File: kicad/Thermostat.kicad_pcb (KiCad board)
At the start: 4 copper layers, 82 x 46 mm, 5 parts, among them J1 Conn_02x20_Odd_Even, U3 XIAO-ESP32-C6-SMD

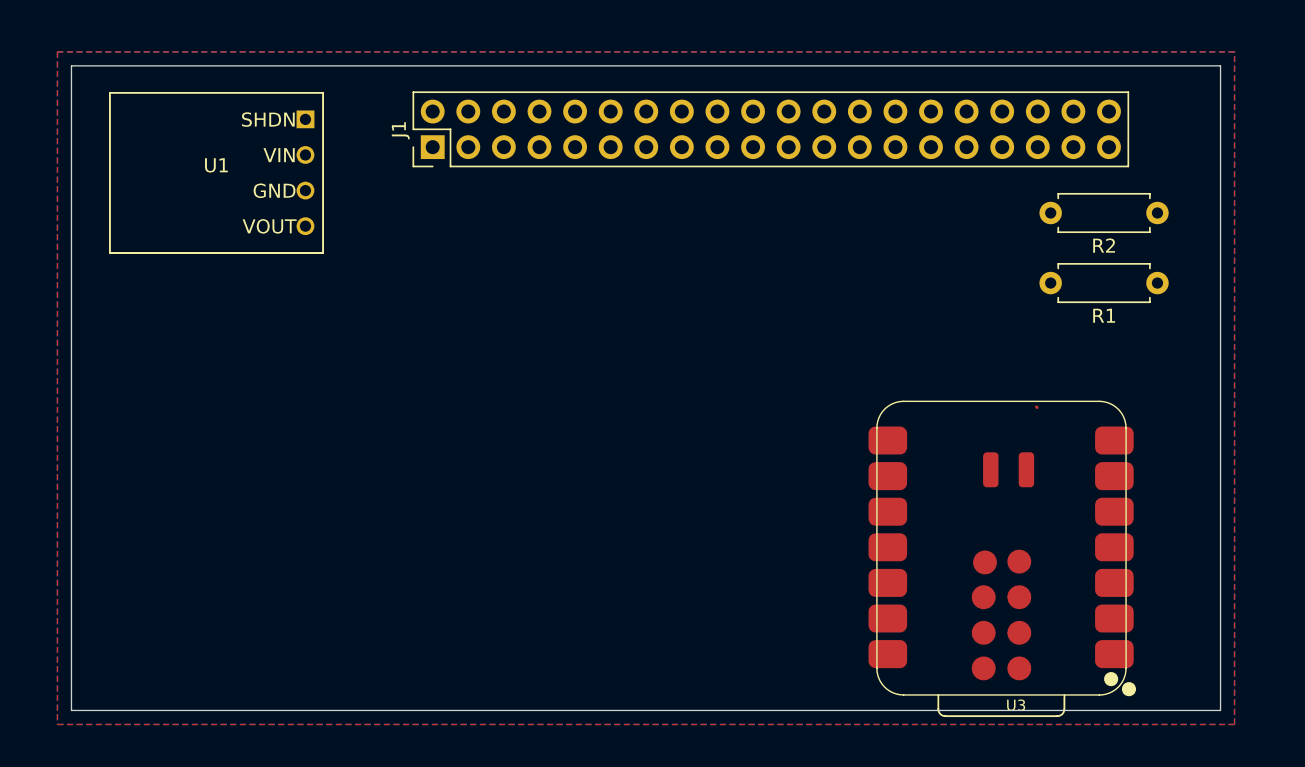
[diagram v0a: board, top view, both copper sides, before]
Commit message: hat header position
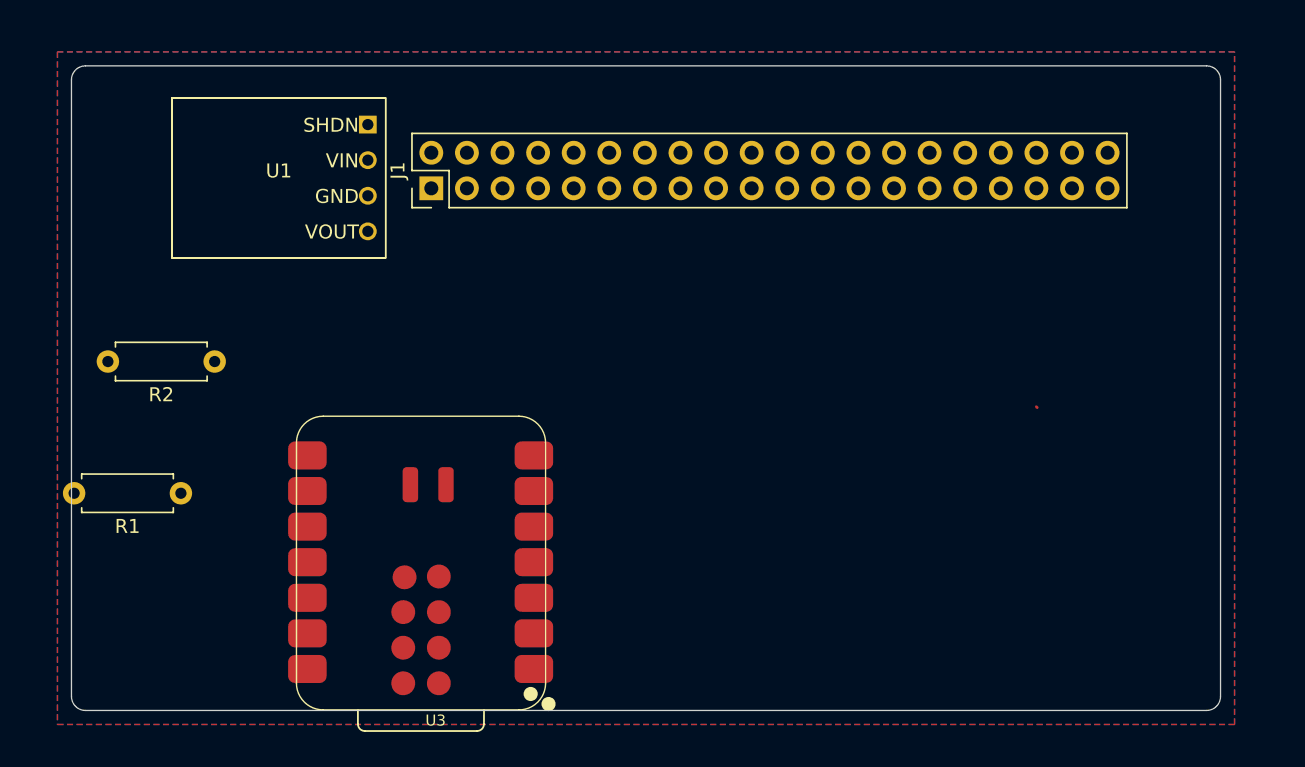
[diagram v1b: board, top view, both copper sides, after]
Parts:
- moved R1 71.3 mm to (76.8, 133.5)
- moved R2 68.1 mm to (79.2, 124.1)
- moved U3 41.4 mm to (102.8, 127.9)
- moved U1 4.47 mm to (83.8, 111.0)
- moved J1 2.94 mm to (94.7, 111.7)
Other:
- outline, holes or cut-outs redrawn
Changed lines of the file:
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@@
 		(13 "F.Paste" user)
 		(15 "B.Paste" user)
-		(5 "F.SilkS" user)
-		(7 "B.SilkS" user)
+		(5 "F.SilkS" user "F.Silkscreen")
+		(7 "B.SilkS" user "B.Silkscreen")
 		(1 "F.Mask" user)
 		(3 "B.Mask" user)
 		(25 "Edge.Cuts" user)
 		(27 "Margin" user)
-		(31 "F.CrtYd" user)
-		(29 "B.CrtYd" user)
+		(31 "F.CrtYd" user "F.Courtyard")
+		(29 "B.CrtYd" user "B.Courtyard")
 		(35 "F.Fab" user)
 	)
@@
 		(capping no)
 		(filling no)
-		(zone_defaults)
 		(pcbplotparams
 			(layerselection 0x00000000_00000000_55555555_5755f5ff)
@@
 	(footprint "Seeed_Studio_XIAO_Series:XIAO-ESP32-C6-SMD"
 		(layer "F.Cu")
-		(at 144.2566 126.8585 180)
+		(at 102.835 127.92 180)
 		(property "Reference" "U3"
 			(at 7.112 -21.336 0)
@@
 		)
 		(property "Value" "XIAO-ESP32-C6-SMD"
-			(at 8.89 -10.795 0)
+			(at 8.6566 -8.7415 0)
 			(layer "F.Fab")
 			(effects
@@
 	(footprint "Resistor_THT:R_Axial_DIN0207_L6.3mm_D2.5mm_P7.62mm_Horizontal"
 		(layer "F.Cu")
-		(at 146.5 113.5 180)
+		(at 79.22 124.1 180)
 		(descr "Resistor, Axial_DIN0207 series, Axial, Horizontal, pin pitch=7.62mm, 0.25W = 1/4W, length*diameter=6.3*2.5mm^2, http://cdn-reichelt.de/documents/datenblatt/B400/1_4W%23YAG.pdf")
 		(tags "Resistor Axial_DIN0207 series Axial Horizontal pin pitch 7.62mm 0.25W = 1/4W length 6.3mm diameter 2.5mm")
@@
 	(footprint "Connector_PinHeader_2.54mm:PinHeader_2x20_P2.54mm_Vertical"
 		(layer "F.Cu")
-		(at 94.78 108.8 90)
+		(at 94.68 111.74 90)
 		(descr "Through hole straight pin header, 2x20, 2.54mm pitch, double rows")
 		(tags "Through hole pin header THT 2x20 2.54mm double row")
@@
 	(footprint "PCM_Pololu:U1V11F5"
 		(layer "F.Cu")
-		(at 79.35 110.63)
+		(at 83.8 111)
 		(property "Reference" "U1"
 			(at 0 -0.5 0)
@@
 			(polygon
 				(pts
-					(xy 71.73 104.915) (xy 86.97 104.915) (xy 86.97 116.345) (xy 71.73 116.345)
+					(xy 76.18 105.285) (xy 91.42 105.285) (xy 91.42 116.715) (xy 76.18 116.715)
 				)
 			)
@@
 	(footprint "Resistor_THT:R_Axial_DIN0207_L6.3mm_D2.5mm_P7.62mm_Horizontal"
 		(layer "F.Cu")
-		(at 146.5 118.5 180)
+		(at 76.81 133.5 180)
 		(descr "Resistor, Axial_DIN0207 series, Axial, Horizontal, pin pitch=7.62mm, 0.25W = 1/4W, length*diameter=6.3*2.5mm^2, http://cdn-reichelt.de/documents/datenblatt/B400/1_4W%23YAG.pdf")
 		(tags "Resistor Axial_DIN0207 series Axial Horizontal pin pitch 7.62mm 0.25W = 1/4W length 6.3mm diameter 2.5mm")
@@
 	)
 	(gr_line
-		(start 69 103)
-		(end 69 149)
+		(start 69 104)
+		(end 69 148)
 		(stroke
 			(width 0.05)
@@
 		(layer "Edge.Cuts")
 	)
-	(gr_line
-		(start 69 149)
-		(end 151 149)
+	(gr_arc
+		(start 69 104)
+		(mid 69.292893 103.292893)
+		(end 70 103)
 		(stroke
 			(width 0.05)
@@
 		(layer "Edge.Cuts")
 	)
-	(gr_line
-		(start 151 103)
-		(end 69 103)
+	(gr_arc
+		(start 70 149)
+		(mid 69.292893 148.707107)
+		(end 69 148)
 		(stroke
 			(width 0.05)
@@
 	)
 	(gr_line
-		(start 151 149)
-		(end 151 103)
+		(start 70 149)
+		(end 150 149)
 		(stroke
 			(width 0.05)
+			(type default)
+		)
+		(layer "Edge.Cuts")
+	)
+	(gr_line
+		(start 150 103)
+		(end 70 103)
+		(stroke
+			(width 0.05)
+			(type default)
+		)
+		(layer "Edge.Cuts")
+	)
+	(gr_arc
+		(start 150 103)
+		(mid 150.707107 103.292893)
+		(end 151 104)
+		(stroke
+			(width 0.05)
+			(type default)
+		)
+		(layer "Edge.Cuts")
+	)
+	(gr_arc
+		(start 151 148)
+		(mid 150.707107 148.707107)
+		(end 150 149)
+		(stroke
+			(width 0.05)
+			(type default)
+		)
+		(layer "Edge.Cuts")
+	)
+	(gr_line
+		(start 151 148)
+		(end 151 104)
+		(stroke
+			(width 0.05)

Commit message: PCB physical layout
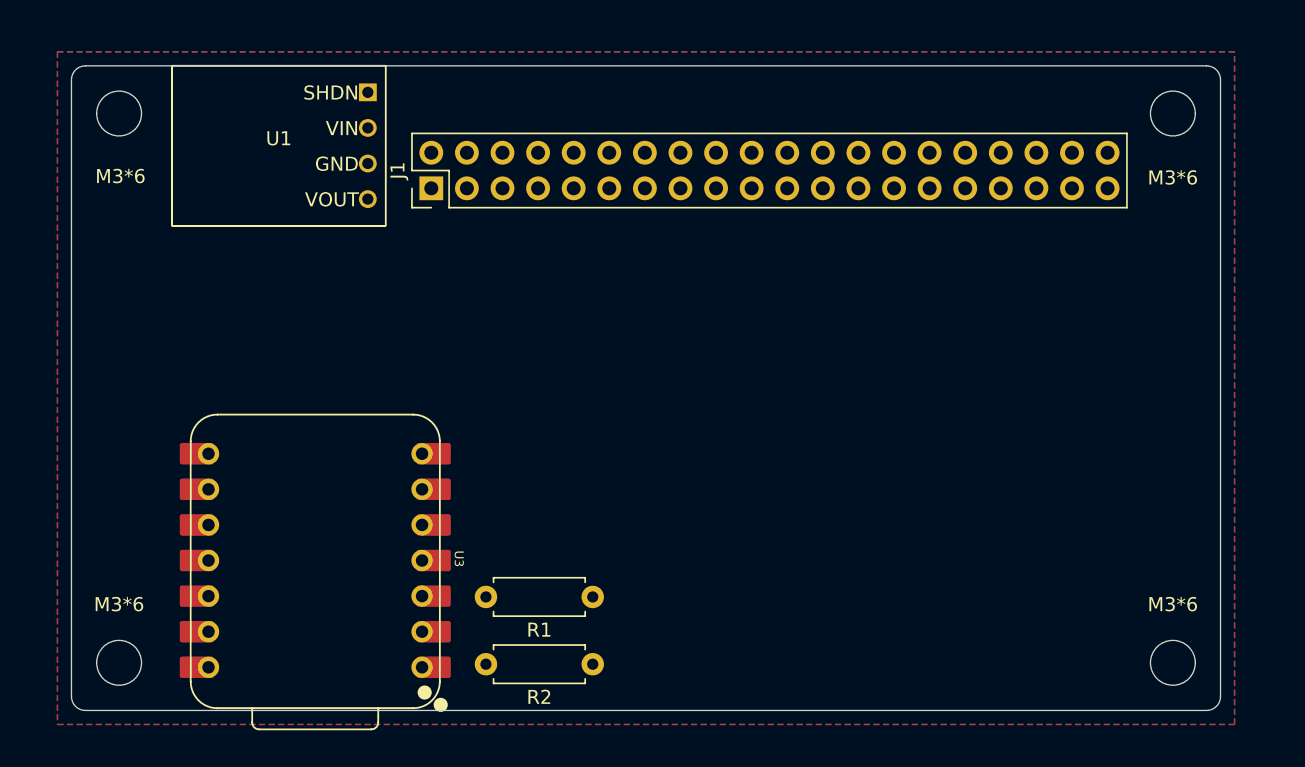
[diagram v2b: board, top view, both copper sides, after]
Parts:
- added M3*6: MountingHole_3.2mm_M3, MountingHole:MountingHole_3.2mm_M3, F.Cu at (72.4, 106.4)
- added M3*6: MountingHole_3.2mm_M3, MountingHole:MountingHole_3.2mm_M3, F.Cu at (147.6, 106.4)
- added M3*6: MountingHole_3.2mm_M3, MountingHole:MountingHole_3.2mm_M3, F.Cu at (147.6, 145.6)
- added M3*6: MountingHole_3.2mm_M3, MountingHole:MountingHole_3.2mm_M3, F.Cu at (72.4, 145.6)
- U3: value XIAO-ESP32-C6-SMD -> XIAO-ESP32-C6-DIP; footprint Seeed_Studio_XIAO_Series:XIAO-ESP32-C6-SMD -> Seeed Studio:XIAO-ESP32-C6-DIP
- moved R2 34.6 mm to (106.2, 145.7)
- moved R1 30.3 mm to (106.2, 140.9)
- moved U3 19.4 mm to (86.4, 138.3), turned to -90 degrees
- moved U1 2.30 mm to (83.8, 108.7)
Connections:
- U3 pad 4: /TCH_RST -> unconnected-(U3-MTDO-Pad16)
- U3 pad 6: /SCL -> unconnected-(U3-MTDI-Pad15)
- U3 pad 7: /INT -> unconnected-(U3-3V3_OUT-Pad22)

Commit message: add battery connector
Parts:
- added J2: Conn_01x02, Connector_Wire:SolderWire-1.5sqmm_1x02_P6mm_D1.7mm_OD3mm_Relief2x, F.Cu at (71.5, 123.9)
- U3: value XIAO-ESP32-C6-DIP -> XIAO-ESP32-C6-SMD; footprint Seeed Studio:XIAO-ESP32-C6-DIP -> Seeed Studio:XIAO-ESP32-C6-SMD
- moved R2 29.4 mm to (78.6, 135.5)
- moved R1 27.6 mm to (78.6, 140.4)
- moved U3 18.3 mm to (101.5, 127.9), turned to 180 degrees
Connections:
- U3 pad 4: unconnected-(U3-MTDO-Pad16) -> /TCH_RST
- U3 pad 6: unconnected-(U3-MTDI-Pad15) -> /SCL
- U3 pad 7: unconnected-(U3-3V3_OUT-Pad22) -> /INT

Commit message: working on pcb
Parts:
- +: renamed from J2; footprint Connector_Wire:SolderWire-1.5sqmm_1x02_P6mm_D1.7mm_OD3mm_Relief2x -> Connector_Wire:SolderWire-0.25sqmm_1x02_P4.2mm_D0.65mm_OD1.7mm_Relief
- moved R1 5.72 mm to (79.1, 134.7)
- moved R2 5.72 mm to (79.1, 129.8)
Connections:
- net Net-(U3-D0) renamed /VSENSE
- + pad 1: -BATT -> +BATT
- + pad 2: +BATT -> -BATT

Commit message: cleanup
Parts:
- renumbered + to J2
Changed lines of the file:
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@@
 		(descr "Soldered wire connection with feed through strain relief, for 2 times 0.25 mm² wires, basic insulation, conductor diameter 0.65mm, outer diameter 1.7mm, size source Multi-Contact FLEXI-E_0.25 (https://www.staubli.com/content/dam/ecs/catalogs-brochures/TM/CAB-Main-11014119-en.pdf#page=9), bend radius 3 times outer diameter")
 		(tags "connector wire 0.25sqmm strain-relief")
-		(property "Reference" "+"
+		(property "Reference" "J2"
 			(at -2.3 0 90)
 			(layer "F.SilkS")

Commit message: traces complete
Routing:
- net /CS: track 0.00 -> 77.5 mm
- net /CLK: track 0.00 -> 62.9 mm
- net /MOSI: track 0.00 -> 62.9 mm
- net /DC: track 0.00 -> 56.8 mm
- net GND: track 0.00 -> 55.9 mm, vias 0 -> 1
- net /RST: track 0.00 -> 43.7 mm
- net /BSY: track 0.00 -> 42.1 mm
- net /VSENSE: track 0.00 -> 39.4 mm, vias 0 -> 1
- net /3V3: track 0.00 -> 39.3 mm
- net +BATT: track 0.00 -> 36.5 mm, vias 0 -> 1
- net -BATT: track 0.00 -> 35.1 mm, vias 0 -> 1
- net /TCH_RST: track 0.00 -> 32.8 mm
- net /SDA: track 0.00 -> 25.6 mm
- net /INT: track 0.00 -> 23.8 mm
- net /SCL: track 0.00 -> 22.6 mm
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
